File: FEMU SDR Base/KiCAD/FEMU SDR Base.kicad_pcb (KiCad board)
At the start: 4 copper layers, 164.8 x 164.8 mm, 105 parts, among them M1 M1, M10 M1, M11 M1, M12 M1, M13 M1, M14 M1, M15 M1, M16 M1, M17 1pin, M18 1pin, M2 M1, M3 M1, M4 M1, M5 M1, M6 M1, M7 M1, M8 M1, M9 M1, P1 Battery, P10 PWM2, P11 PWM3, P12 PWM4, P13 PWM1, P14 PWM2, P15 PWM3, P16 PWM4, P17 12V, P18 GND, P19 12V, P2 SDR_Shield_1, P20 GND, P21 SDR0, P22 SDR1, P27 PWM0, P28 PWM5, P29 PWM6, P3 SDR_Shield_2, P30 PWM7, P31 PWM0, P32 PWM5, P33 PWM6, P34 PWM7, P35 Battery, P36 RPi, P37 PXH, P38 Rx, P4 12V, P5 GND, P6 12V, P7 GND, P8 Raspi_Power_Shield, P9 PWM1, U1 TPS562209, U2 LP38858-LDO, U3 LP38858-LDO, U4 LM1117, U5 LM1117

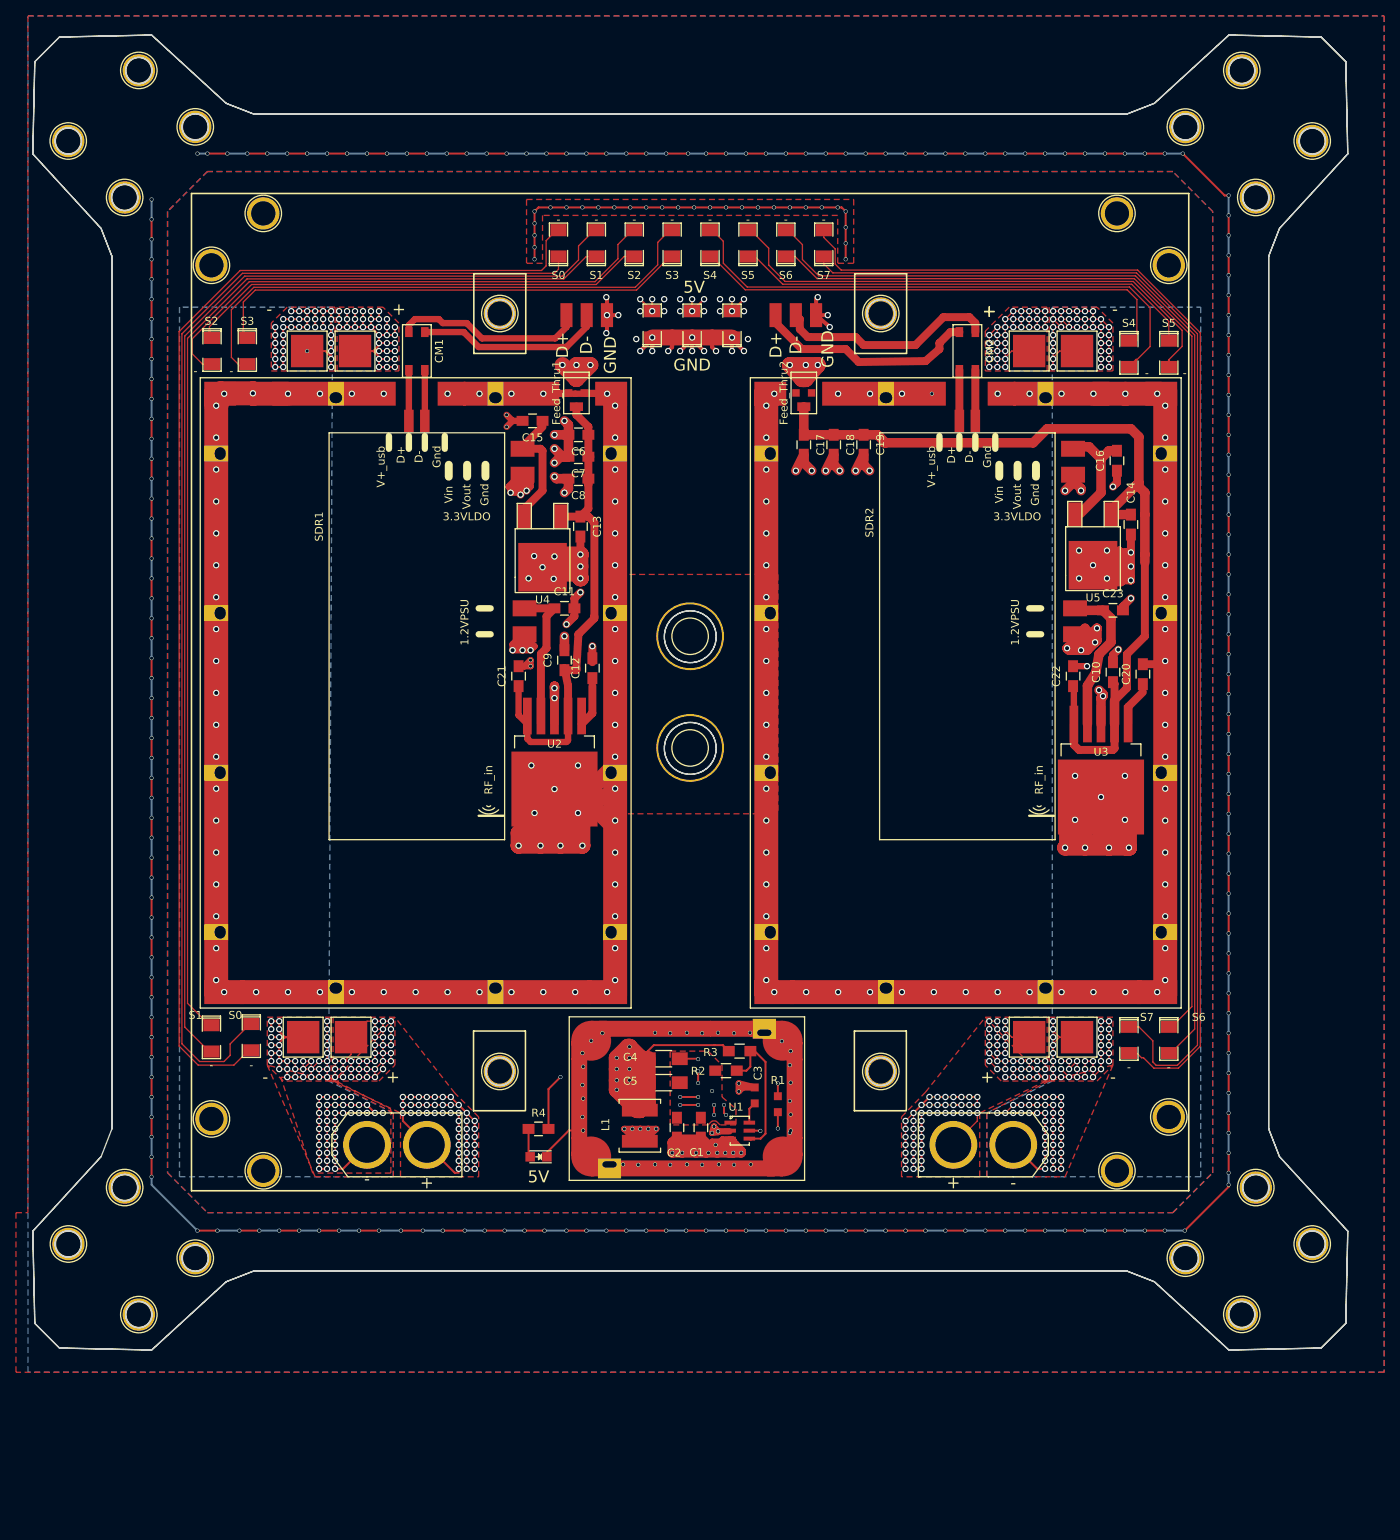
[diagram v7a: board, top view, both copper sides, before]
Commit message: Status=Free, Ground -12V overlap fixed on power pins, stitching vias made smaller to stay within Seeed manufacturing limits, cable tray vias all connected to ground, bottom silkscreen overlap of text fixed
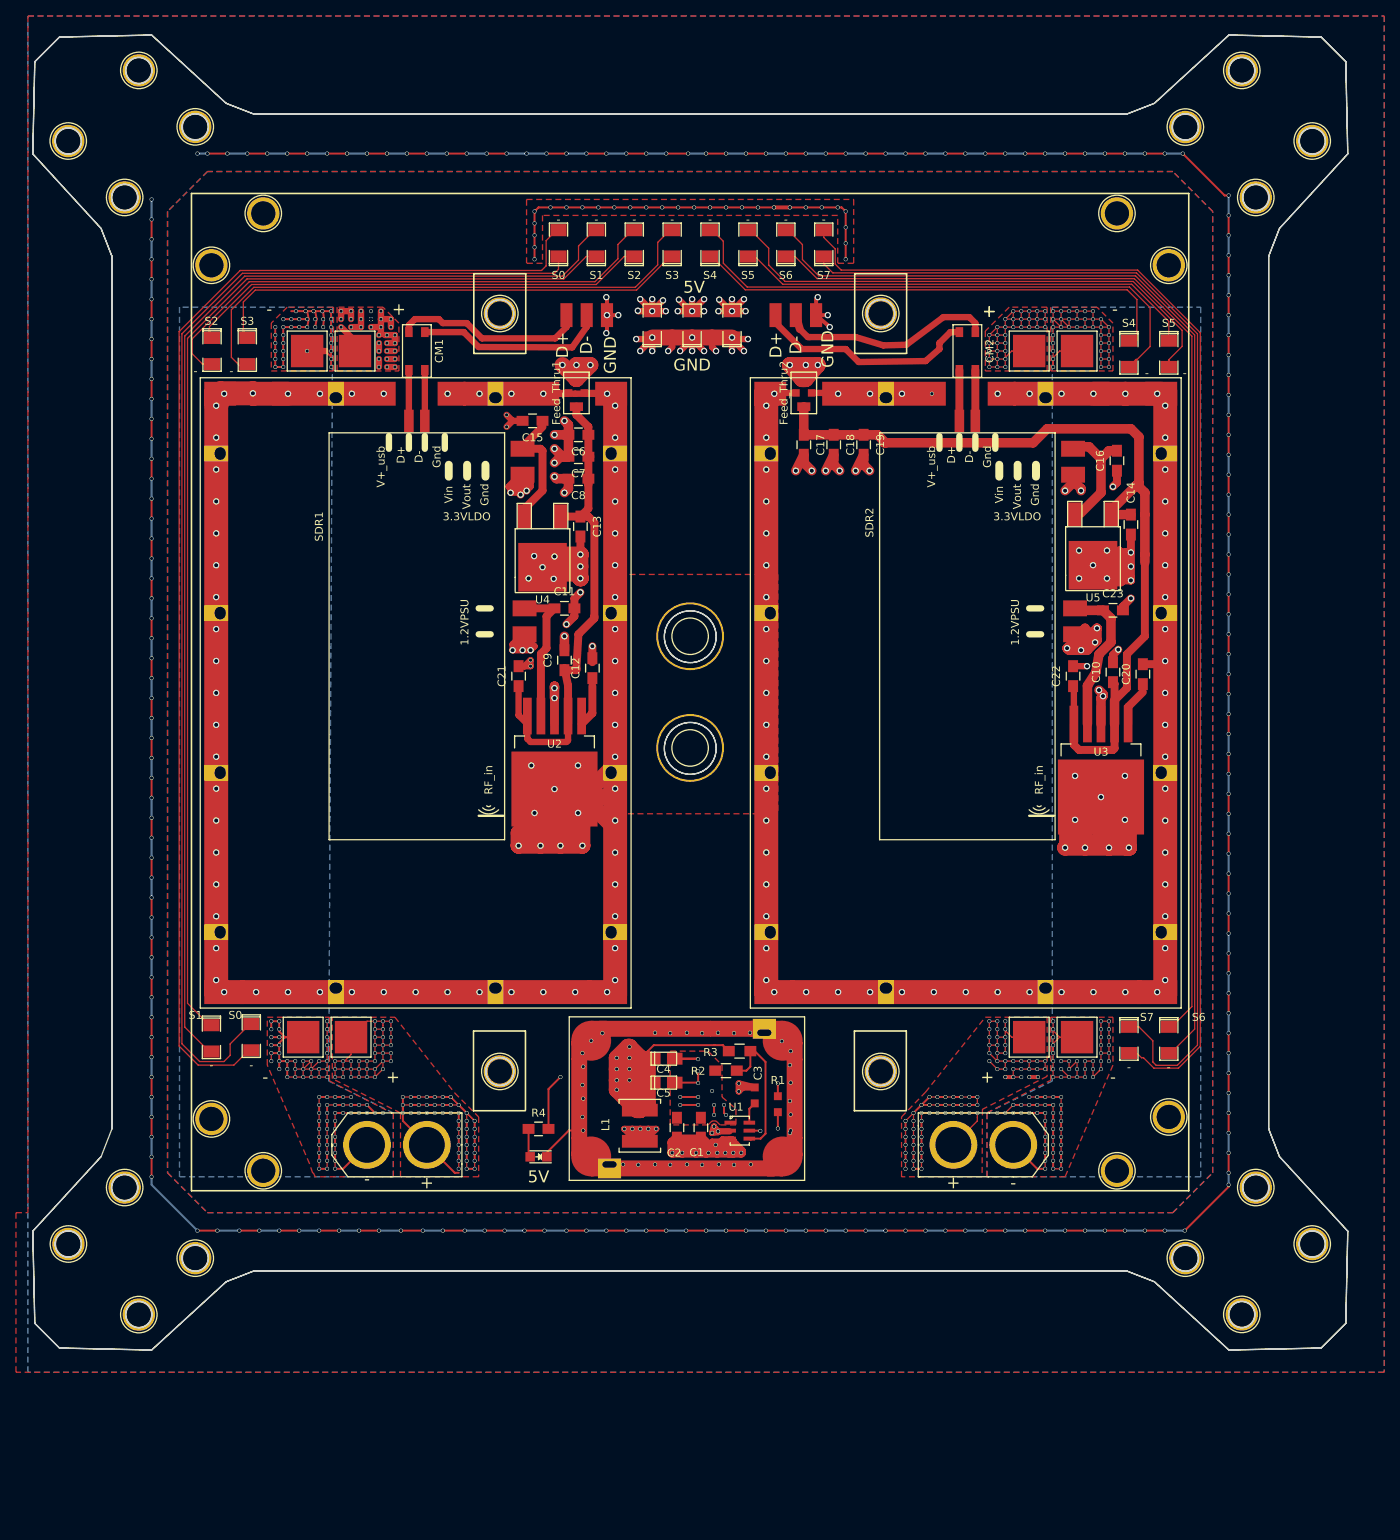
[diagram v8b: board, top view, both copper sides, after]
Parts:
- C4, C5: footprint Capacitors_SMD:C_1206_HandSoldering -> Capacitors_Tantalum_SMD:TantalC_SizeS_EIA-3216
- M17: value 1pin -> SMA1
- M18: value 1pin -> SMA2
- turned C4 to 180 degrees
- turned C5 to 180 degrees
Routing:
- net GND: track 1965.7 -> 1996.7 mm, vias 705 -> 713
- net +5V: track 283.2 -> 297.5 mm
- net (no net): track 6.00 -> 0.00 mm, vias 13 -> 0
- net +12V: track 350.6 -> 352.7 mm
- net Net-(CM2-Pad1): track 27.7 -> 27.0 mm
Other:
- rule trace_min: 0.13 -> 0.149
- board text added: "/\ /\ RF goes here"
- board text removed: "RF goes here ->"
